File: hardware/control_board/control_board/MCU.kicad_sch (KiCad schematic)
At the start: 32 parts, among them J2 Conn_01x05_Pin, Q1 AO3401A, U1 STM32F411CEUx, Y1 25MHz, Y2 32.768kHz

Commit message: feat：EEPROM原理图
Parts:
- added C13: 100nF, Capacitor_SMD:C_0603_1608Metric, symbol Device:C
- added R6, R7, R8: 4.7kR, Resistor_SMD:R_0603_1608Metric, symbol Device:R
- added U2: M24C64, Package_SO:SOIC-8_3.9x4.9mm_P1.27mm, symbol Memory_EEPROM:M24C64
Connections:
- net +3.3V: now also C13.1, R6.2, R7.2, R8.2, U2.8 (VCC)
- net GND: now also C13.2, U2.1 (A0), U2.2 (A1), U2.3 (A2), U2.4 (GND)
- net IIC_SCL: now also U1.42 (PB6), R7.1, U2.6 (SCL); no longer U1.43 (PB7)
- net IIC_SDA: now also U1.43 (PB7), R8.1, U2.5 (SDA); no longer U1.42 (PB6)
- net ROM_WP: now reaches U1.41 (PB5)
- net ROM_WP: now also R6.1, U2.7 (WP)

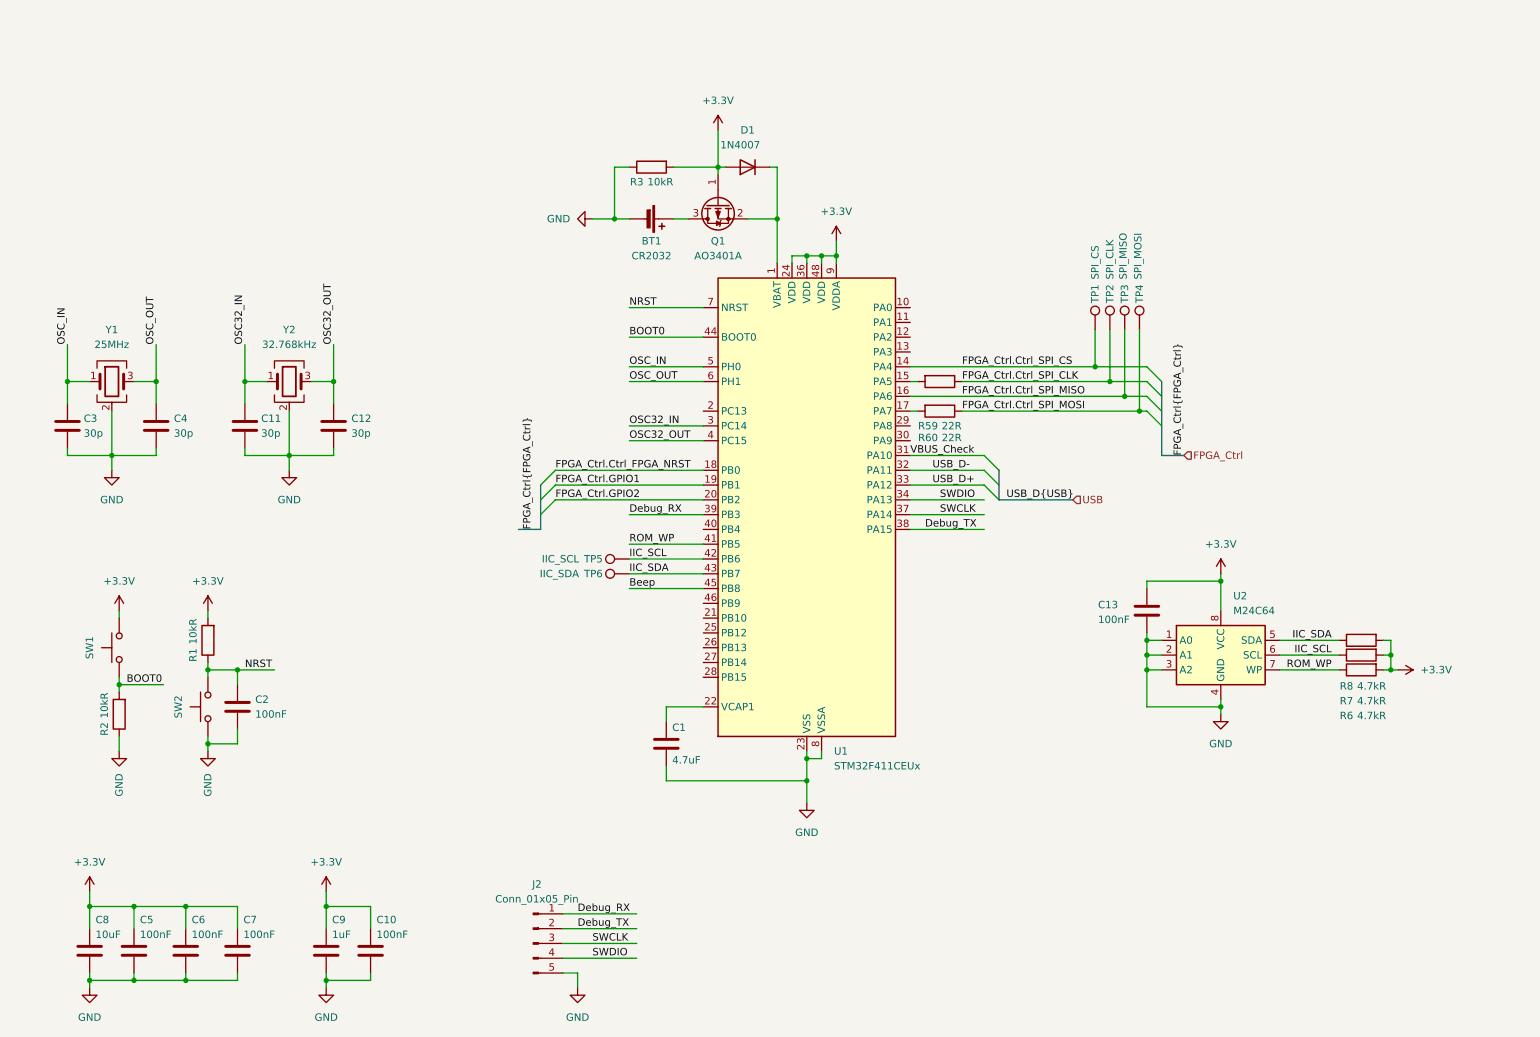
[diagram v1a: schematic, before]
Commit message: feat：控制板电源原理图
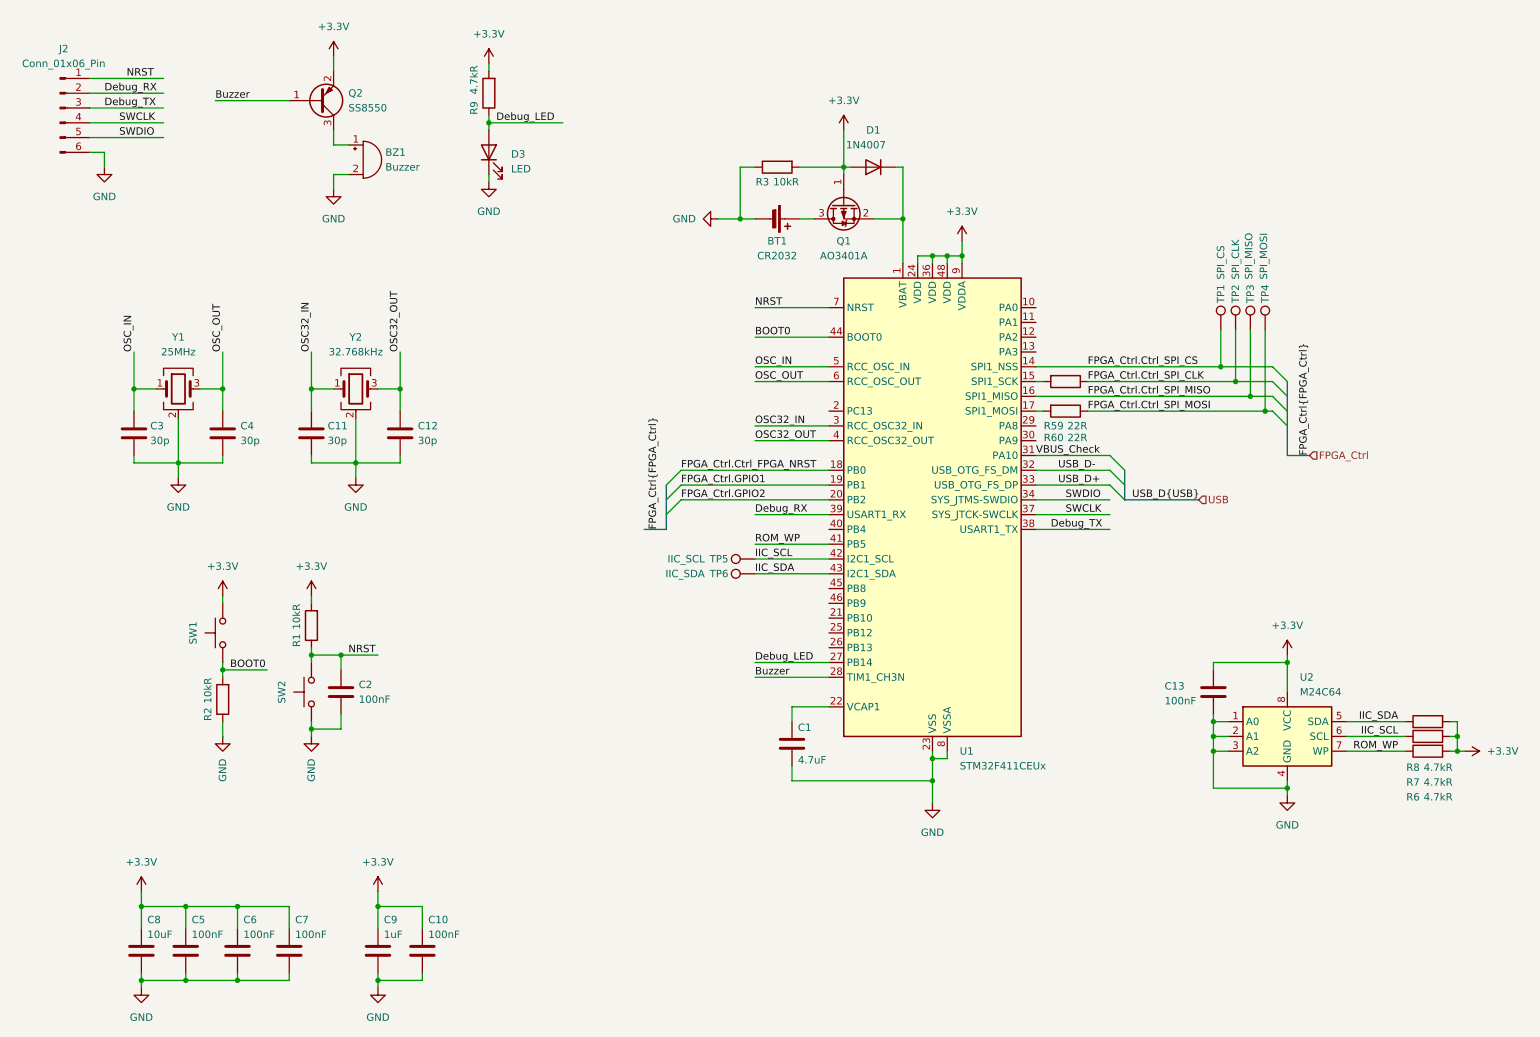
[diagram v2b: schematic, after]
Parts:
- removed J2: Conn_01x05_Pin, Connector_PinHeader_2.54mm:PinHeader_1x05_P2.54mm_Vertical, symbol Connector:Conn_01x05_Pin
- added BZ1: Buzzer, symbol Device:Buzzer
- added D3: LED, LED_SMD:LED_0603_1608Metric, symbol Device:LED
- added J2: Conn_01x06_Pin, Connector_PinHeader_2.54mm:PinHeader_1x06_P2.54mm_Vertical, symbol Connector:Conn_01x06_Pin
- added Q2: SS8550, Package_TO_SOT_SMD:SOT-23, symbol Transistor_BJT:SS8550
- added R9: 4.7kR, Resistor_SMD:R_0603_1608Metric, symbol Device:R
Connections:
- net +3.3V: now also Q2.2 (E), R9.2
- net Debug_RX: now also J2.2 (Pin_2)
- net Debug_TX: now also J2.3 (Pin_3)
- net GND: now also BZ1.2 (-), D3.1 (K), J2.6 (Pin_6)
- net NRST: now also J2.1 (Pin_1)
- net SWCLK: now also J2.4 (Pin_4)
- net SWDIO: now also J2.5 (Pin_5)
- net Debug_LED: now reaches U1.27 (PB14)
- net Debug_LED: now also D3.2 (A), R9.1
- net Buzzer: now reaches U1.28 (PB15)
- net Buzzer: now also Q2.1 (B)
- net Beep: no longer names the net of U1.45 (PB8)
- new net: BZ1.1 (+), Q2.3 (C)
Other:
- moved on the sheet: BT1, C1, C10, C11, C12, C13, C2, C3, C4, C5, C6, C7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

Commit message: debug：蜂鸣器驱动电路；debug LED；电源输出排针
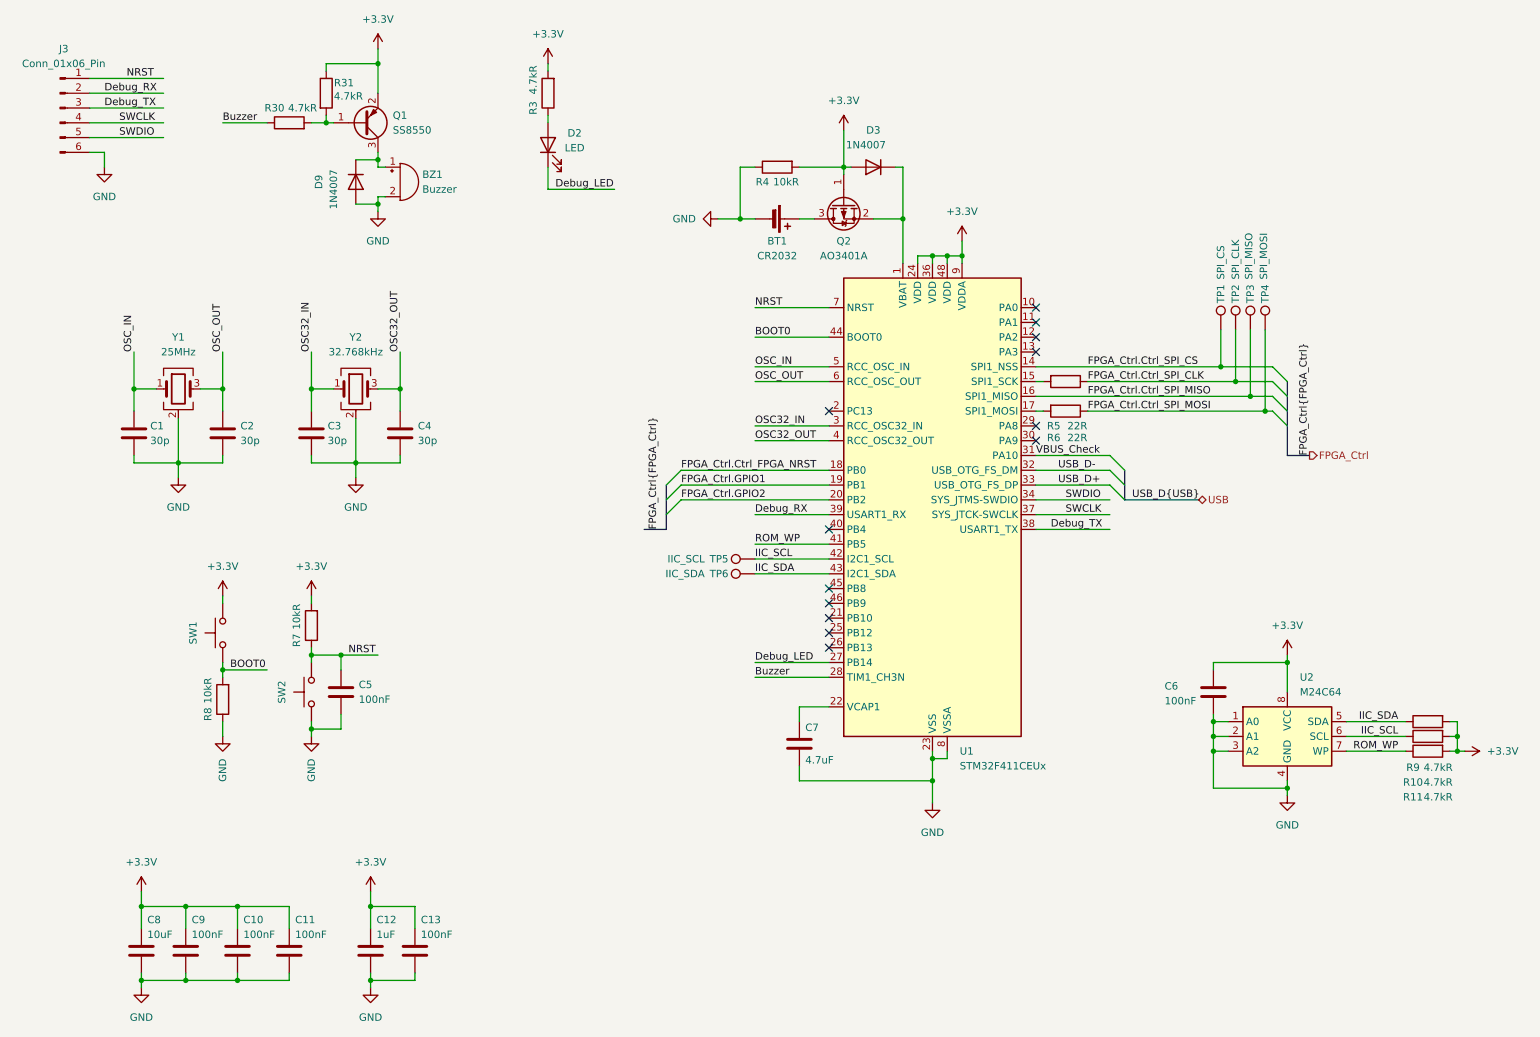
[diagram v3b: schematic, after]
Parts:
- added D9: 1N4007, Diode_SMD:D_SOD-123, symbol Diode:1N4007
- added R30, R31: 4.7kR, Resistor_SMD:R_0603_1608Metric, symbol Device:R
- BZ1: footprint (none) -> Buzzer_Beeper:MagneticBuzzer_StarMicronics_QMX
- D3: renamed from D1; footprint Diode_SMD:D_SMA -> Diode_SMD:D_SOD-123
- SW1, SW2: value (none) -> SW_MEC_5G
- renumbered C3 to C1, C6 to C10, C7 to C11, C9 to C12, C10 to C13, C4 to C2, C11 to C3, C12 to C4, C2 to C5, C13 to C6, C1 to C7, C5 to C9, D3 to D2, J2 to J3, Q2 to Q1, Q1 to Q2, R7 to R10, R6 to R11, R9 to R3, R3 to R4, R59 to R5, R60 to R6, R1 to R7, R2 to R8, R8 to R9
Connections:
- net +3.3V: now also SW1.2 (B), R31.1; no longer SW1.3 (B), SW1.4 (B)
- net BOOT0: no longer SW1.2 (A)
- net Buzzer: now also R30.1; no longer Q1.1 (B)
- net Debug_LED: now also D2.1 (K); no longer D2.2 (A), R3.1
- net GND: now also D9.2 (A); no longer D2.1 (K), SW2.2 (A)
- net NRST: now also SW2.2 (B); no longer SW2.3 (B), SW2.4 (B)
- net at BZ1.1 (+), Q1.3 (C): now also D9.1 (K)
- new net: Q1.1 (B), R30.2, R31.2
- new net: D2.2 (A), R3.1
- no-connect marks 0 -> 13
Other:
- moved on the sheet: BZ1, C12, C13, C7, D2, Q1, R3

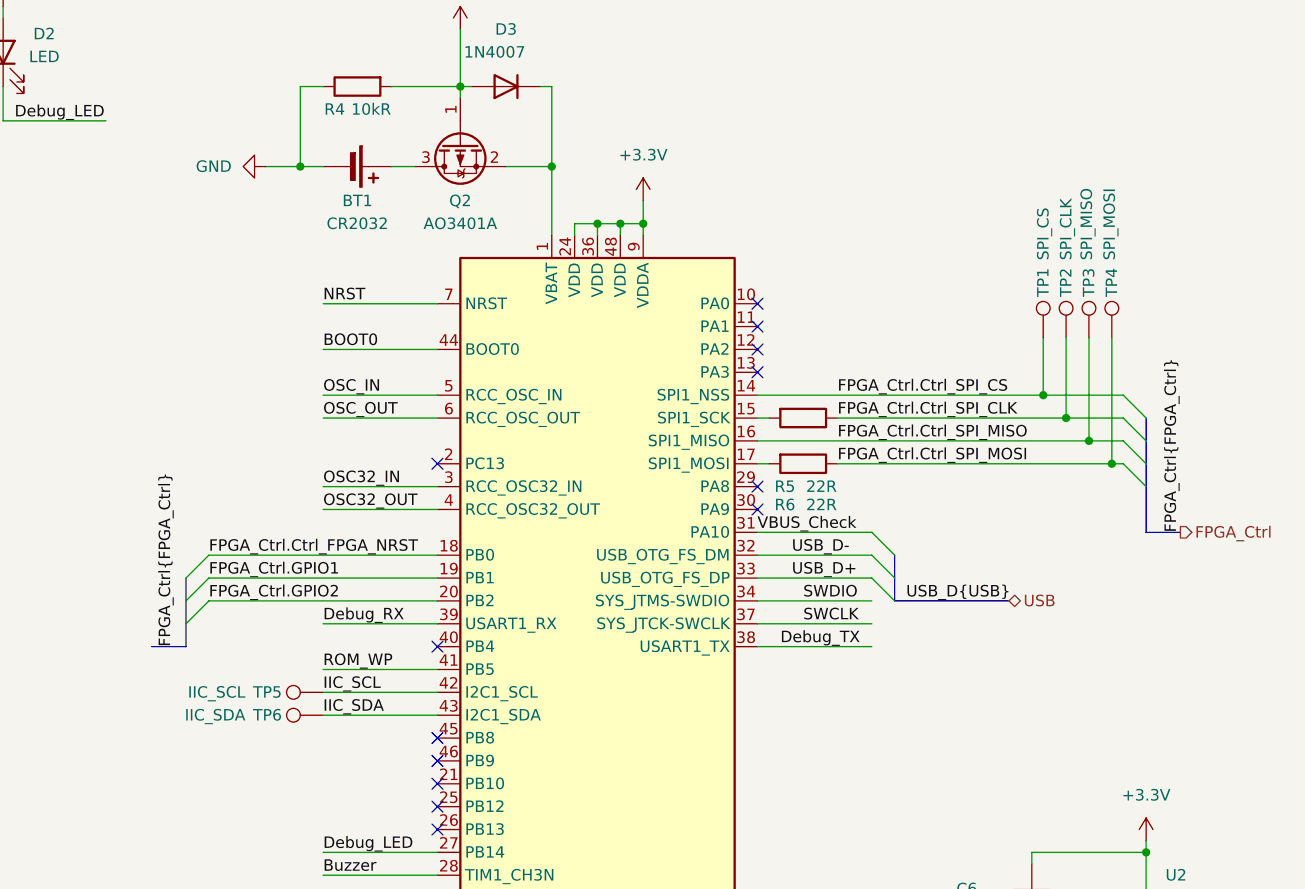
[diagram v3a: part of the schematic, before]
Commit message: feat：根据PCB微调原理图
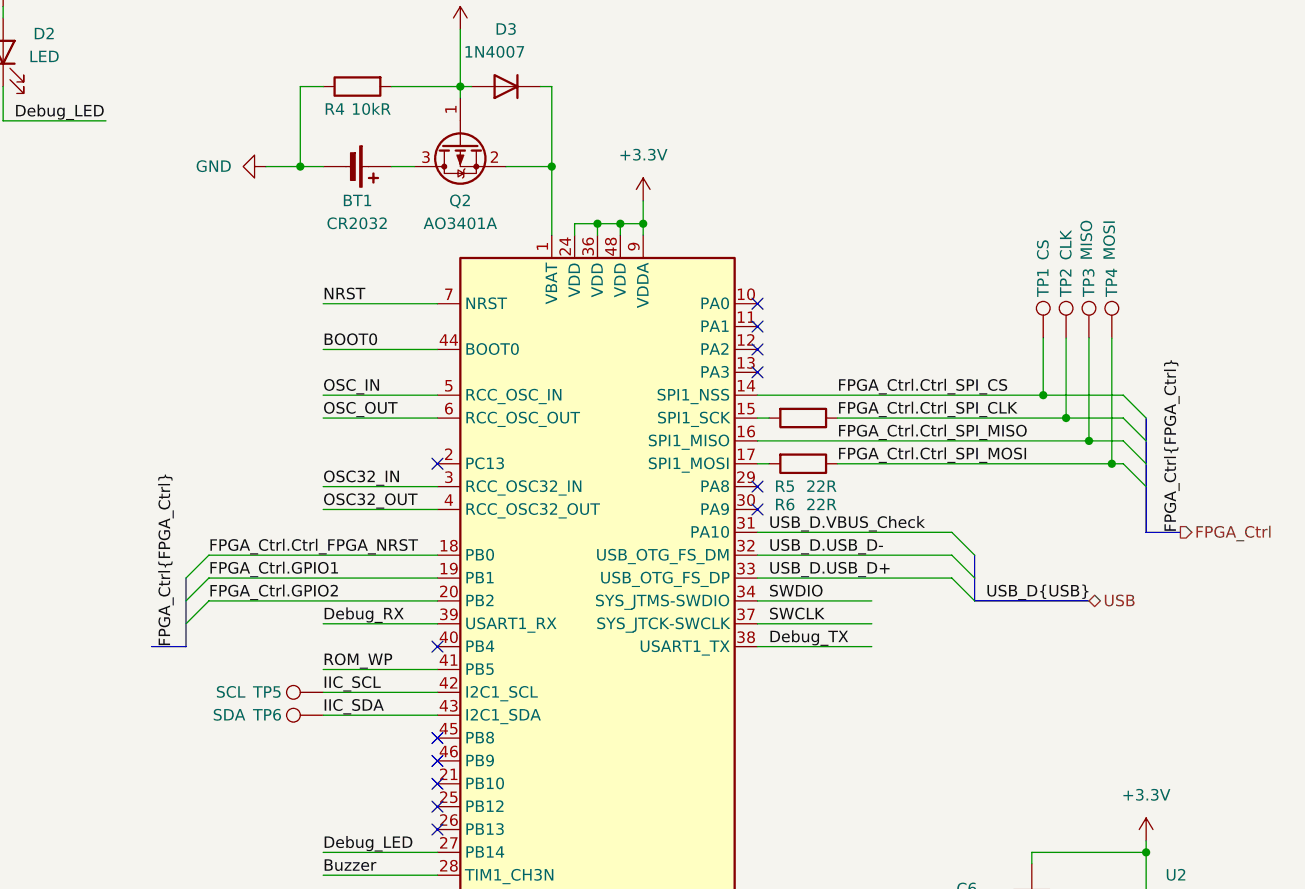
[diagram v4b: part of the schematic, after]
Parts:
- SW1: value SW_MEC_5G -> BOOT0
- SW2: value SW_MEC_5G -> NRST
- TP1: value SPI_CS -> CS
- TP2: value SPI_CLK -> CLK
- TP3: value SPI_MISO -> MISO
- TP4: value SPI_MOSI -> MOSI
- TP5: value IIC_SCL -> SCL
- TP6: value IIC_SDA -> SDA
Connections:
- net USB_D+ renamed USB_D.USB_D+
- net USB_D- renamed USB_D.USB_D-
- net VBUS_Check renamed USB_D.VBUS_Check
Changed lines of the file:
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@@
 	)
 	(bus_entry
-		(at 207.01 95.25)
+		(at 215.9 95.25)
 		(size 2.54 2.54)
 		(stroke
@@
 	)
 	(bus_entry
-		(at 207.01 97.79)
+		(at 215.9 97.79)
 		(size 2.54 2.54)
 		(stroke
@@
 	)
 	(bus_entry
-		(at 207.01 92.71)
+		(at 215.9 92.71)
 		(size 2.54 2.54)
 		(stroke
@@
 	(wire
 		(pts
+			(xy 194.31 92.71) (xy 215.9 92.71)
+		)
+		(stroke
+			(width 0)
+			(type default)
+		)
+	)
+	(wire
+		(pts
 			(xy 171.45 52.07) (xy 171.45 59.69)
 		)
@@
 	(wire
 		(pts
-			(xy 194.31 97.79) (xy 207.01 97.79)
+			(xy 194.31 97.79) (xy 215.9 97.79)
 		)
 		(stroke
@@
 	(bus
 		(pts
-			(xy 209.55 100.33) (xy 222.25 100.33)
+			(xy 218.44 100.33) (xy 231.14 100.33)
 		)
 		(stroke
@@
 	(bus
 		(pts
-			(xy 209.55 95.25) (xy 209.55 100.33)
+			(xy 218.44 95.25) (xy 218.44 100.33)
 		)
 		(stroke
@@
 	(wire
 		(pts
-			(xy 194.31 92.71) (xy 207.01 92.71)
-		)
-		(stroke
-			(width 0)
-			(type default)
-		)
-	)
-	(wire
-		(pts
 			(xy 77.47 86.36) (xy 77.47 93.98)
 		)
@@
 	(wire
 		(pts
-			(xy 194.31 95.25) (xy 207.01 95.25)
+			(xy 194.31 95.25) (xy 215.9 95.25)
 		)
 		(stroke
@@
 	)
 	(label "SWDIO"
-		(at 199.39 100.33 0)
+		(at 195.58 100.33 0)
 		(effects
 			(font
@@
 		)
 	)
-	(label "USB_D+"
-		(at 198.12 97.79 0)
+	(label "USB_D.USB_D+"
+		(at 195.58 97.79 0)
 		(effects
 			(font
@@
 		)
 	)
-	(label "USB_D-"
-		(at 198.12 95.25 0)
+	(label "USB_D.USB_D-"
+		(at 195.58 95.25 0)
 		(effects
 			(font
@@
 		)
 	)
-	(label "VBUS_Check"
-		(at 194.31 92.71 0)
+	(label "USB_D.VBUS_Check"
+		(at 195.58 92.71 0)
 		(effects
 			(font
@@
 	)
 	(label "SWCLK"
-		(at 199.39 102.87 0)
+		(at 195.58 102.87 0)
 		(effects
 			(font
@@
 	)
 	(label "USB_D{USB}"
-		(at 210.82 100.33 0)
+		(at 219.71 100.33 0)
 		(effects
 			(font
@@
 	)
 	(label "Debug_TX"
-		(at 196.85 105.41 0)
+		(at 195.58 105.41 0)
 		(effects
 			(font
@@
 	(hierarchical_label "USB"
 		(shape bidirectional)
-		(at 222.25 100.33 0)
+		(at 231.14 100.33 0)
 		(effects
 			(font
@@
 			)
 		)
-		(property "Value" "SPI_MISO"
+		(property "Value" "MISO"
 			(at 230.886 62.484 90)
 			(show_name no)
@@
 			)
 		)
-		(property "Value" "SPI_CS"
+		(property "Value" "CS"
 			(at 226.06 62.484 90)
 			(show_name no)
@@
 			)
 		)
-		(property "Value" "SW_MEC_5G"
+		(property "Value" "BOOT0"
 			(at 49.53 123.19 0)
 			(hide yes)
@@
 			)
 		)
-		(property "Value" "IIC_SCL"
+		(property "Value" "SCL"
 			(at 137.414 110.49 90)
 			(show_name no)
@@
 			)
 		)
-		(property "Value" "IIC_SDA"
+		(property "Value" "SDA"
 			(at 137.414 113.03 90)
 			(show_name no)
@@
 			)
 		)
-		(property "Value" "SPI_MOSI"
+		(property "Value" "MOSI"
 			(at 233.426 62.484 90)
 			(show_name no)
@@
 			)
 		)
-		(property "Value" "SPI_CLK"
+		(property "Value" "CLK"
 			(at 228.6 62.484 90)
 			(show_name no)
@@
 			)
 		)
-		(property "Value" "SW_MEC_5G"
+		(property "Value" "NRST"
 			(at 64.77 133.35 0)
 			(hide yes)
